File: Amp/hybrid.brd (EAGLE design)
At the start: 172.7 x 137.2 mm, 139 parts, among them IC1 TL071P, IC2 TL071P, IC3 LM317MABT, IC4 LM317MABT, J1 NRJ3HF-1, K1 UA2-12NJ, Q1 KSP06KINKED, Q10 BD139, Q11 KSP06KINKED, Q12 BC560KINKED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

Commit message: Small adjustments
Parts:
- IC1, IC2: device linear:DIL08 -> my-ic:DIL08
- moved IC4 5.08 mm to (165.1, 114.3)
- moved R44 5.08 mm to (16.5, 114.3)
- moved IC3 5.08 mm to (7.62, 114.3)
- moved C27 5.08 mm to (25.4, 109.2), turned to 0 degrees
- moved R47 5.08 mm to (156.2, 114.3)
- moved C25 4.02 mm to (26.7, 114.3), turned to 180 degrees
- moved R48 3.81 mm to (152.4, 114.3)
- moved R43 3.81 mm to (20.3, 114.3)
- moved C30 1.27 mm to (147.3, 124.5)
- moved C31 1.27 mm to (148.6, 119.4)
- moved J1 1.27 mm to (57.1, 1.27)
- turned C29 to 180 degrees
- turned C32 to 0 degrees
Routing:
- net HT: track 269.0 -> 261.2 mm
- net VCC: track 544.1 -> 537.7 mm
- net N$37: track 47.8 -> 42.7 mm
- net OUT_R: track 141.4 -> 137.4 mm
- net N$36: track 26.5 -> 22.6 mm
- net +LV: track 97.9 -> 94.9 mm
- net OUT_R*: track 20.7 -> 21.8 mm
- net OUT_L*: track 29.1 -> 28.6 mm

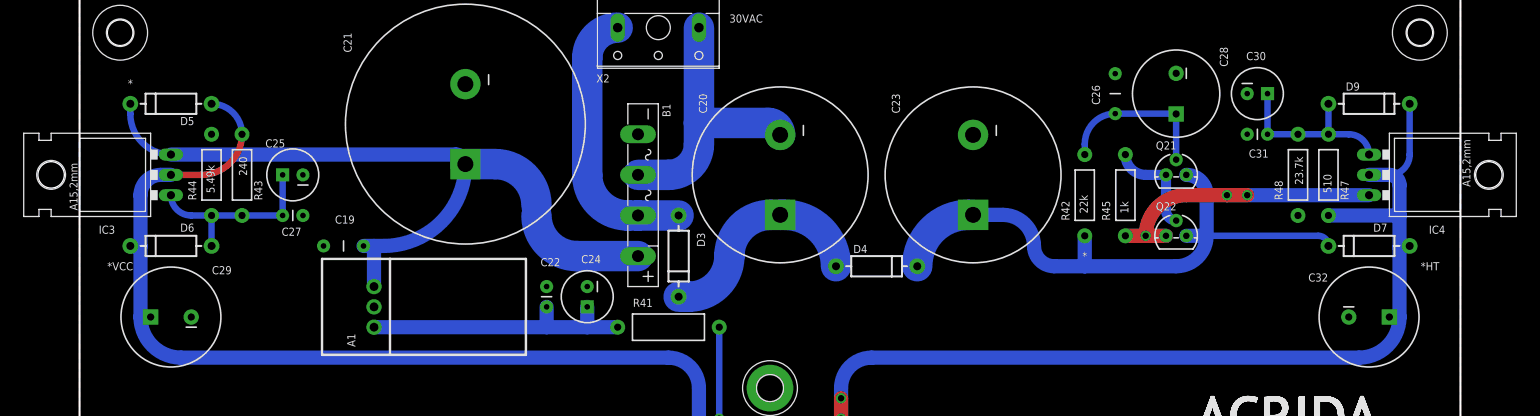
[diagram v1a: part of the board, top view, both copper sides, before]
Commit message: TO-220 redrawn for perfect fit into grid
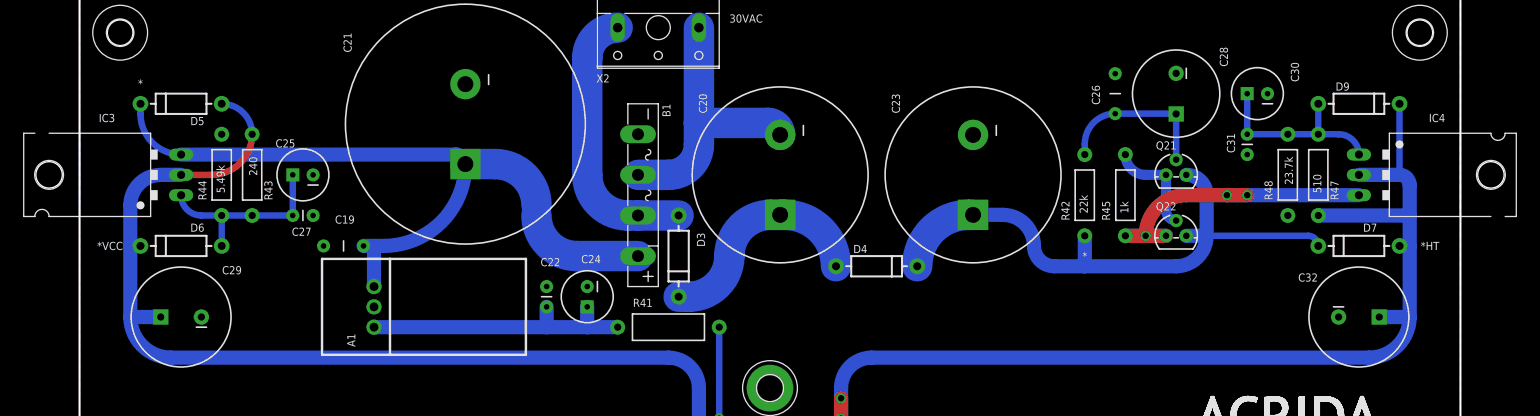
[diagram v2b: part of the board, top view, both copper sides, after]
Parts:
- moved C31 2.54 mm to (146.1, 119.4), turned to 270 degrees
- moved R47 1.27 mm to (154.9, 114.3)
- moved R48 1.27 mm to (151.1, 114.3)
- moved C27 1.27 mm to (26.7, 109.2)
- moved C25 1.27 mm to (27.9, 114.3)
- moved C29 1.27 mm to (12.7, 96.5)
- moved D5 1.27 mm to (12.7, 123.2)
- moved D6 1.27 mm to (12.7, 105.4)
- moved R43 1.27 mm to (21.6, 114.3)
- moved R44 1.27 mm to (17.8, 114.3)
- moved C32 1.27 mm to (160.0, 96.5)
- moved D7 1.27 mm to (160.0, 105.4)
- moved D9 1.27 mm to (160.0, 123.2)
- turned C30 to 180 degrees
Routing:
- net HT: track 261.2 -> 269.0 mm
- net VCC: track 537.7 -> 543.3 mm
- net N$33: track 73.9 -> 72.6 mm
- net +LV: track 94.9 -> 93.7 mm
- net N$36: track 22.6 -> 23.9 mm
- net N$37: track 42.7 -> 41.5 mm

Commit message: Small adjustments
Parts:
- moved X2 2.54 mm to (72.4, 129.5)
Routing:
- net AC_2: track 34.6 -> 32.0 mm
- net AC_1: track 33.5 -> 31.0 mm
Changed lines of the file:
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@@
 <attribute name="VALUE" x="118.11" y="33.528" size="1.27" layer="27" ratio="10" rot="R180"/>
 </element>
-<element name="X2" library="con-wago-508" package="W237-2N" value="" x="72.39" y="132.08" smashed="yes" rot="R180">
-<attribute name="MF" value="" x="72.39" y="132.08" size="1.778" layer="27" ratio="20" rot="R180" display="off"/>
-<attribute name="MPN" value="" x="72.39" y="132.08" size="1.778" layer="27" ratio="20" rot="R180" display="off"/>
-<attribute name="NAME" x="64.643" y="125.857" size="1.016" layer="25" ratio="19"/>
-<attribute name="OC_FARNELL" value="unknown" x="72.39" y="132.08" size="1.778" layer="27" ratio="20" rot="R180" display="off"/>
-<attribute name="OC_NEWARK" value="unknown" x="72.39" y="132.08" size="1.778" layer="27" ratio="20" rot="R180" display="off"/>
-<attribute name="VALUE" x="78.74" y="136.398" size="1.27" layer="27" ratio="10" rot="R180"/>
+<element name="X2" library="con-wago-508" package="W237-2N" value="" x="72.39" y="129.54" smashed="yes" rot="R180">
+<attribute name="MF" value="" x="72.39" y="129.54" size="1.778" layer="27" ratio="20" rot="R180" display="off"/>
+<attribute name="MPN" value="" x="72.39" y="129.54" size="1.778" layer="27" ratio="20" rot="R180" display="off"/>
+<attribute name="NAME" x="64.643" y="123.317" size="1.016" layer="25" ratio="19"/>
+<attribute name="OC_FARNELL" value="unknown" x="72.39" y="129.54" size="1.778" layer="27" ratio="20" rot="R180" display="off"/>
+<attribute name="OC_NEWARK" value="unknown" x="72.39" y="129.54" size="1.778" layer="27" ratio="20" rot="R180" display="off"/>
+<attribute name="VALUE" x="78.74" y="133.858" size="1.27" layer="27" ratio="10" rot="R180"/>
 </element>
 <element name="Q21" library="my-tran" package="TO-92" value="KSP43" x="137.16" y="114.3" smashed="yes">
@@
 <wire x1="77.47" y1="118.11" x2="73.66" y2="114.3" width="3.81" layer="16" curve="-90"/>
 <wire x1="77.47" y1="120.797778125" x2="77.47" y2="118.11" width="3.81" layer="16"/>
-<wire x1="77.47" y1="120.797778125" x2="77.47" y2="132.715" width="3.81" layer="16"/>
+<wire x1="77.47" y1="120.797778125" x2="77.47" y2="130.175" width="3.81" layer="16"/>
 <wire x1="87.63" y1="119.3" x2="86.132221875" y2="120.797778125" width="3.81" layer="16" curve="90"/>
 <wire x1="86.132221875" y1="120.797778125" x2="77.47" y2="120.797778125" width="3.81" layer="16"/>
@@
 <contactref element="D3" pad="A"/>
 <contactref element="X2" pad="2"/>
-<wire x1="63.5" y1="128.905" x2="67.31" y2="132.715" width="3.81" layer="16" curve="-90"/>
-<wire x1="63.5" y1="114.3" x2="63.5" y2="128.905" width="3.81" layer="16"/>
 <wire x1="68.58" y1="109.22" x2="69.85" y2="109.22" width="3.81" layer="16"/>
 <wire x1="68.58" y1="109.22" x2="63.5" y2="114.3" width="3.81" layer="16" curve="-90"/>
 <wire x1="69.85" y1="109.22" x2="74.93" y2="109.22" width="3.81" layer="16"/>
+<wire x1="63.5" y1="114.3" x2="63.5" y2="126.365" width="3.81" layer="16"/>
+<wire x1="63.5" y1="126.365" x2="67.31" y2="130.175" width="3.81" layer="16" curve="-90"/>
 </signal>
 <signal name="N$46">
